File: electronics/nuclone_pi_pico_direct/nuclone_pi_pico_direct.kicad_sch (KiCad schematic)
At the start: 22 parts, among them J1 JTAG_2X05, J3 nuclone_medium_left, J4 nuclone_medium_right, SW1 RESET

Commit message: WIP place and route of the board
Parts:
- removed C14: 100n, SquantorCapacitor:C_0603, symbol Device:C
- removed R13: 470, SquantorResistor:R_0603_hand, symbol Device:R
- removed SW1: RESET, SquantorSwitches:TD-85XU, symbol Switch:SW_Push

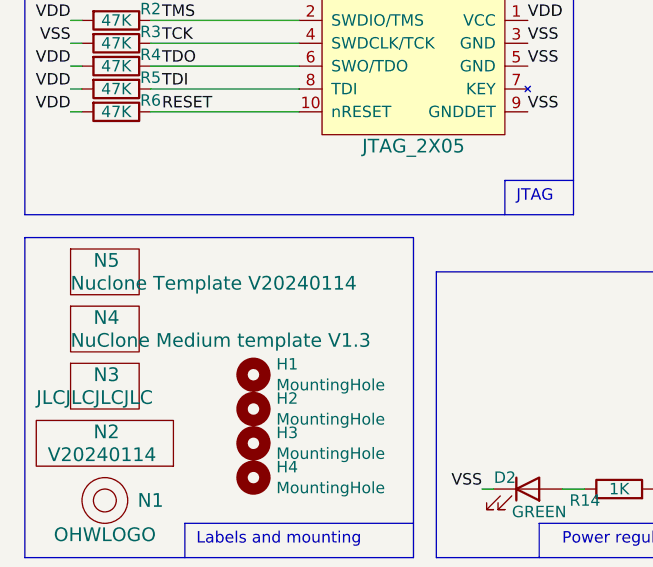
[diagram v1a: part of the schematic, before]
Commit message: updated pinout to match the RP2040 nuclone
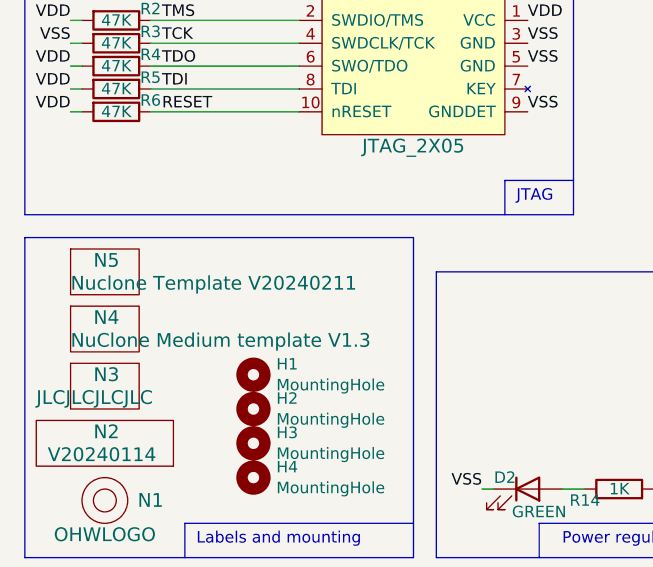
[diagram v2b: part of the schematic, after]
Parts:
- N5: value Nuclone Template V20240114 -> Nuclone Template V20240211
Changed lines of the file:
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@@
       (effects (font (size 1.524 1.524)) (justify left))
     )
-    (property "Value" "Nuclone Template V20240114" (at 20.32 163.83 0)
+    (property "Value" "Nuclone Template V20240211" (at 20.32 163.83 0)
       (effects (font (size 1.524 1.524)) (justify left))
     )

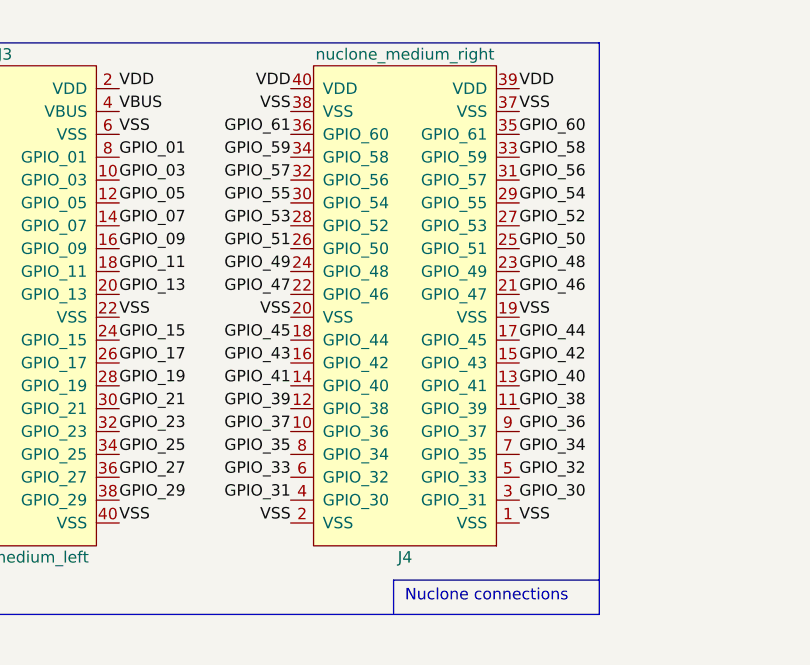
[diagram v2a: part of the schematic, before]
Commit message: fixed pinouts
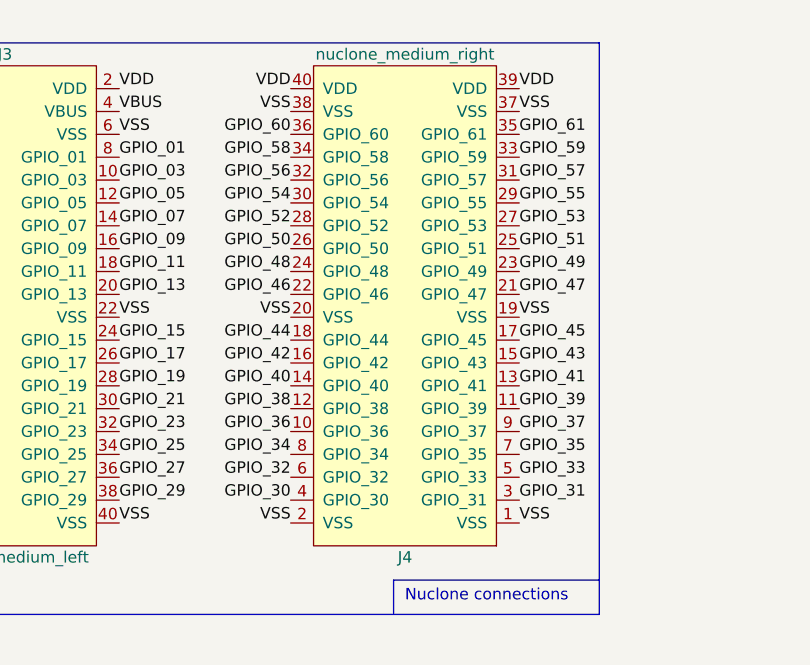
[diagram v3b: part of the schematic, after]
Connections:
- net GPIO_30: now also J4.4 (GPIO_30); no longer J4.3 (GPIO_31)
- net GPIO_31: now also J4.3 (GPIO_31); no longer J4.4 (GPIO_30)
- net GPIO_32: now also J4.6 (GPIO_32); no longer J4.5 (GPIO_33)
- net GPIO_33: now also J4.5 (GPIO_33); no longer J4.6 (GPIO_32)
- net GPIO_34: now also J4.8 (GPIO_34); no longer J4.7 (GPIO_35)
- net GPIO_35: now also J4.7 (GPIO_35); no longer J4.8 (GPIO_34)
- net GPIO_36: now also J4.10 (GPIO_36); no longer J4.9 (GPIO_37)
- net GPIO_37: now also J4.9 (GPIO_37); no longer J4.10 (GPIO_36)
- net GPIO_38: now also J4.12 (GPIO_38); no longer J4.11 (GPIO_39)
- net GPIO_39: now also J4.11 (GPIO_39); no longer J4.12 (GPIO_38)
- net GPIO_40: now also J4.14 (GPIO_40); no longer J4.13 (GPIO_41)
- net GPIO_41: now also J4.13 (GPIO_41); no longer J4.14 (GPIO_40)
- net GPIO_42: now also J4.16 (GPIO_42); no longer J4.15 (GPIO_43)
- net GPIO_43: now also J4.15 (GPIO_43); no longer J4.16 (GPIO_42)
- net GPIO_44: now also J4.18 (GPIO_44); no longer J4.17 (GPIO_45)
- net GPIO_45: now also J4.17 (GPIO_45); no longer J4.18 (GPIO_44)
- net GPIO_46: now also J4.22 (GPIO_46); no longer J4.21 (GPIO_47)
- net GPIO_47: now also J4.21 (GPIO_47); no longer J4.22 (GPIO_46)
- net GPIO_48: now also J4.24 (GPIO_48); no longer J4.23 (GPIO_49)
- net GPIO_49: now also J4.23 (GPIO_49); no longer J4.24 (GPIO_48)
- net GPIO_50: now also J4.26 (GPIO_50); no longer J4.25 (GPIO_51)
- net GPIO_51: now also J4.25 (GPIO_51); no longer J4.26 (GPIO_50)
- net GPIO_52: now also J4.28 (GPIO_52); no longer J4.27 (GPIO_53)
- net GPIO_53: now also J4.27 (GPIO_53); no longer J4.28 (GPIO_52)
- net GPIO_54: now also J4.30 (GPIO_54); no longer J4.29 (GPIO_55)
- net GPIO_55: now also J4.29 (GPIO_55); no longer J4.30 (GPIO_54)
- net GPIO_56: now also J4.32 (GPIO_56); no longer J4.31 (GPIO_57)
- net GPIO_57: now also J4.31 (GPIO_57); no longer J4.32 (GPIO_56)
- net GPIO_58: now also J4.34 (GPIO_58); no longer J4.33 (GPIO_59)
- net GPIO_59: now also J4.33 (GPIO_59); no longer J4.34 (GPIO_58)
- net GPIO_60: now also J4.36 (GPIO_60); no longer J4.35 (GPIO_61)
- net GPIO_61: now also J4.35 (GPIO_61); no longer J4.36 (GPIO_60)

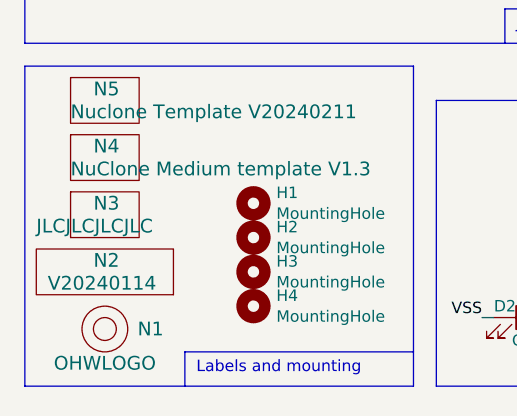
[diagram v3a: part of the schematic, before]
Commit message: prepped nuclone with pi pico module with direct USB connection for production
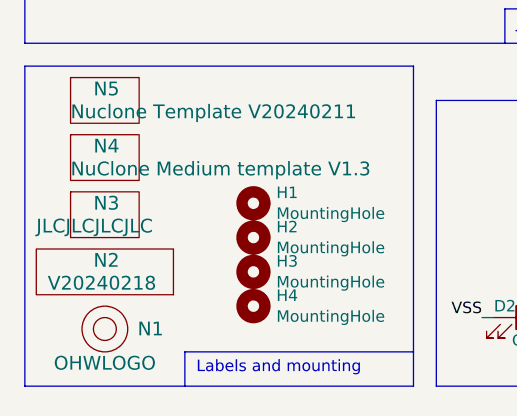
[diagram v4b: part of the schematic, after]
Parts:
- N2: value V20240114 -> V20240218
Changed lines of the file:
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@@
       (effects (font (size 1.524 1.524)) (justify left))
     )
-    (property "Value" "V20240114" (at 17.78 182.88 0)
+    (property "Value" "V20240218" (at 17.78 182.88 0)
       (effects (font (size 1.524 1.524)) (justify left))
     )

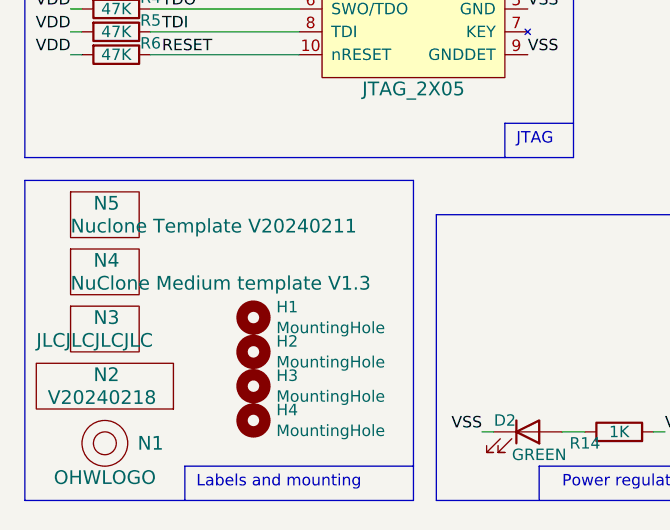
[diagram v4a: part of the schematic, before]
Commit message: updated board description label
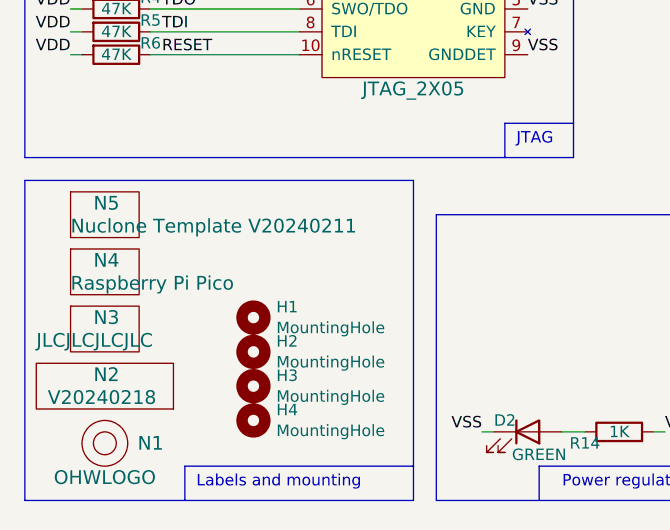
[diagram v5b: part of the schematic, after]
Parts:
- N4: value NuClone Medium template V1.3 -> Raspberry Pi Pico
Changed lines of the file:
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@@
       (effects (font (size 1.524 1.524)) (justify left))
     )
-    (property "Value" "NuClone Medium template V1.3" (at 20.32 170.18 0)
+    (property "Value" "Raspberry Pi Pico" (at 20.32 170.18 0)
       (effects (font (size 1.524 1.524)) (justify left))
     )

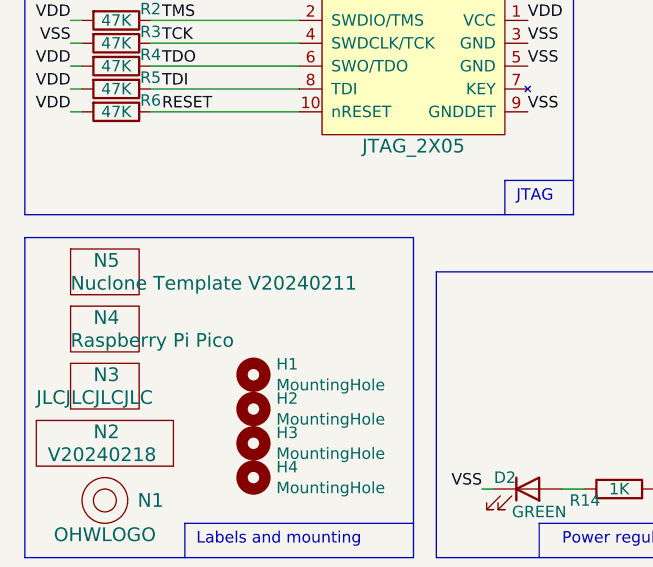
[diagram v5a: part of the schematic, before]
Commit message: preparing for production, updated footprints and versionnumber, redrawn copper layers
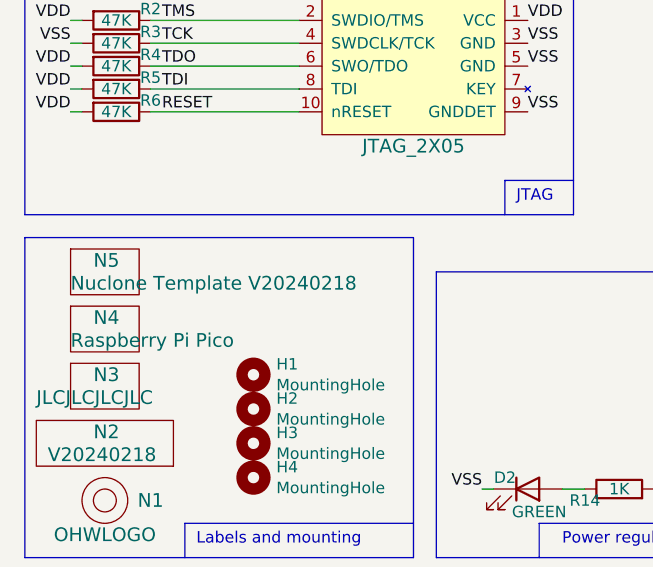
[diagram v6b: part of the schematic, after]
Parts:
- N5: value Nuclone Template V20240211 -> Nuclone Template V20240218
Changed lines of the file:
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@@
       (effects (font (size 1.524 1.524)) (justify left))
     )
-    (property "Value" "Nuclone Template V20240211" (at 20.32 163.83 0)
+    (property "Value" "Nuclone Template V20240218" (at 20.32 163.83 0)
       (effects (font (size 1.524 1.524)) (justify left))
     )
